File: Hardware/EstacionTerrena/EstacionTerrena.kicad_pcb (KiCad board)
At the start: 2 copper layers, 40 x 30 mm, 40 parts, among them J1 5-1814832-1, J2 USB_B_Micro, J3 Conn_01x03, U1 TPD2E2U06, U2 MIC5323-3.3YD5_TR, U3 MCP2210, U4 CC1101RGP, U5 0915BM15A0001E, Y1 12MHz, Y2 26 MHz

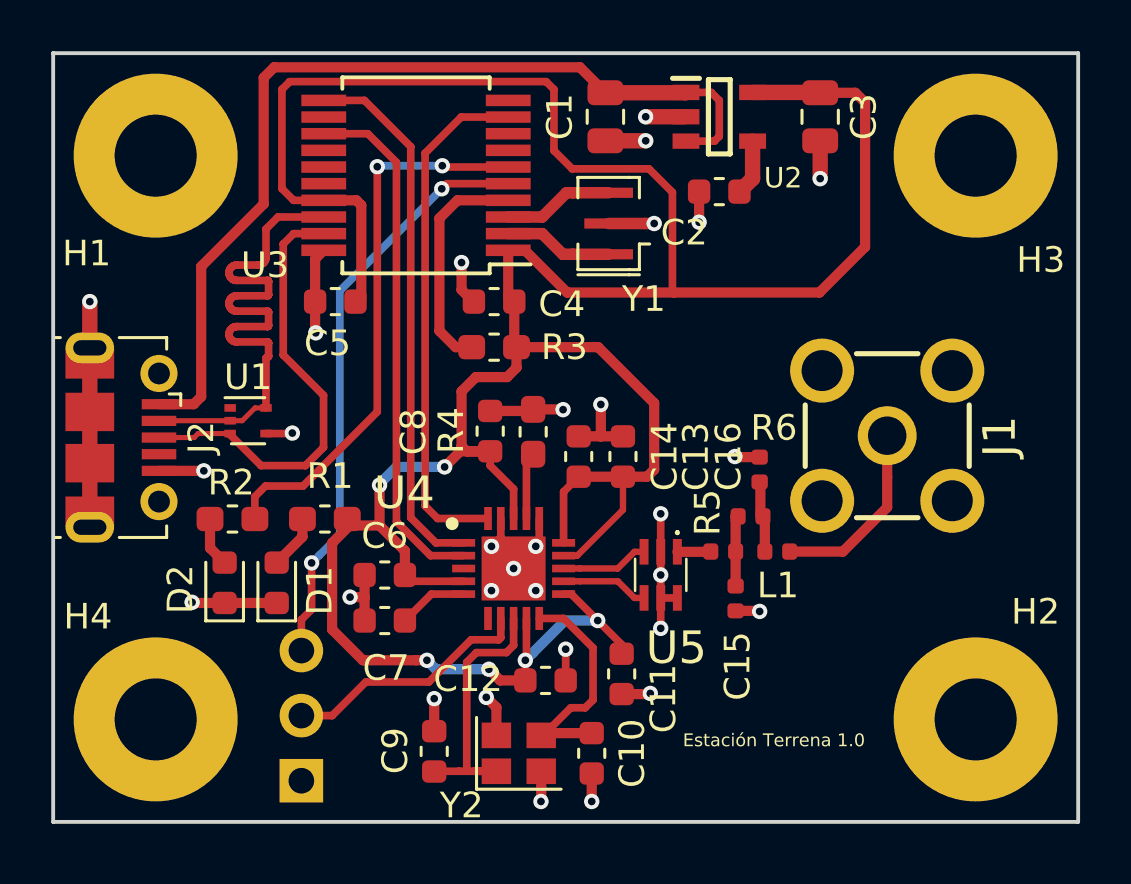
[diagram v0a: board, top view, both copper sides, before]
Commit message: Componentes 0402 en CC1101 PCB estacion terrena
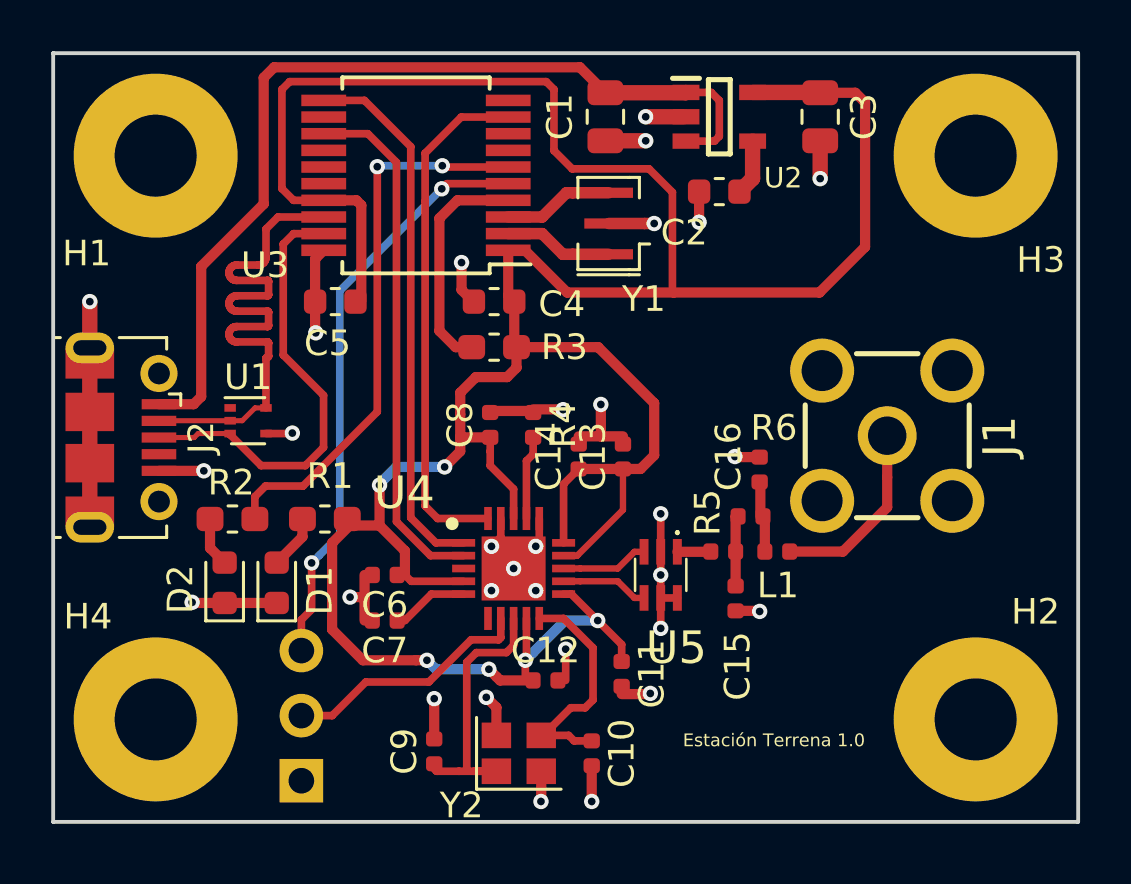
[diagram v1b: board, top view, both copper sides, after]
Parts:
- C10, C11, C12, C13, C14, C6, C7, C8, C9: footprint Capacitor_SMD:C_0603_1608Metric -> Capacitor_SMD:C_0402_1005Metric
- R4: footprint Resistor_SMD:R_0603_1608Metric_Pad1.05x0.95mm_HandSolder -> Resistor_SMD:R_0402_1005Metric
- moved R4 0.27 mm to (18.7, 14.5)
- moved C8 0.24 mm to (17.1, 14.5)
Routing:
- net Net-(R4-Pad2): track 2.63 -> 3.29 mm
